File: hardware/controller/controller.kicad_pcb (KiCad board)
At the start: 4 copper layers, 57 x 47 mm, 46 parts, among them J1 Conn_01x02_Pin, J11 Barrel_Jack, J12 USB_C_Receptacle_USB2.0_14P, J2 Conn_01x02_Pin, J3 Conn_01x02_Pin, J5 Screw_Terminal_01x02, J6 Screw_Terminal_01x02, U1 ESP32-C3-MINI-1, U2 MAX31855KASA, U3 MAX31855KASA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

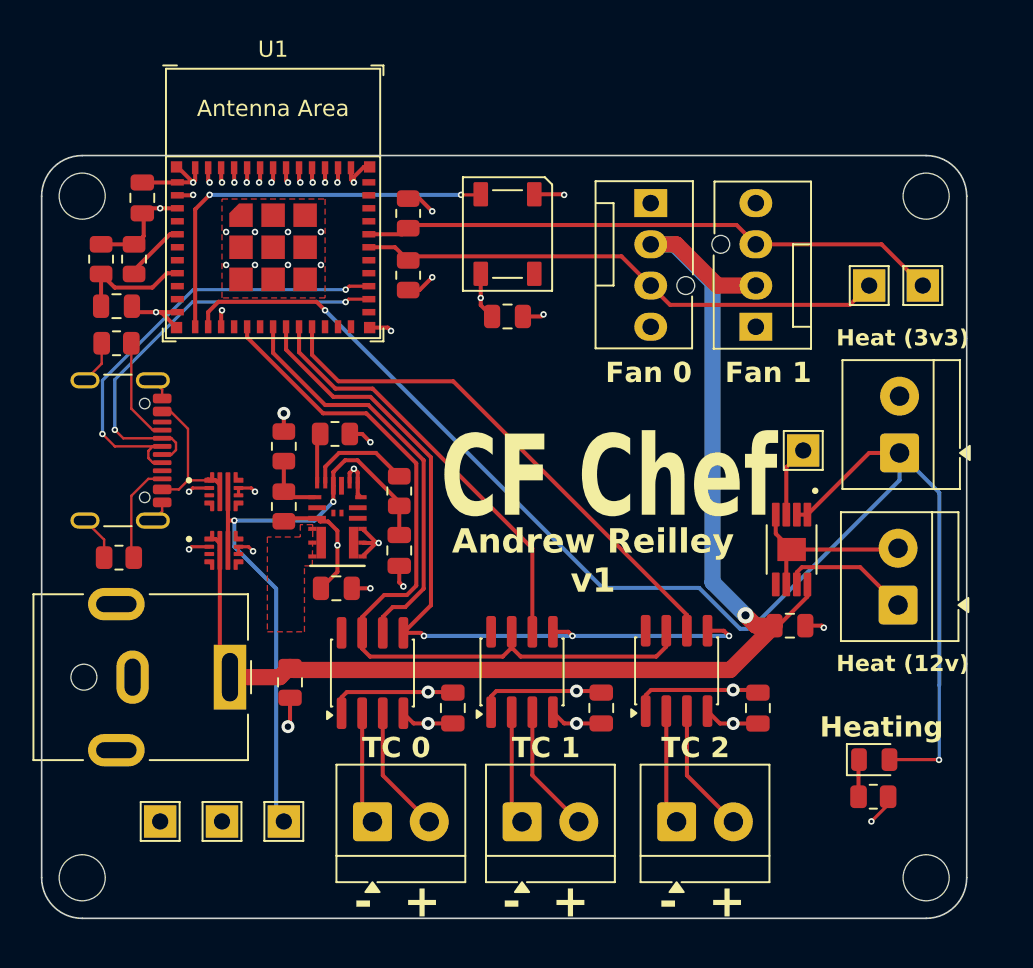
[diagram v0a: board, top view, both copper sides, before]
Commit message: Reroute USB connector
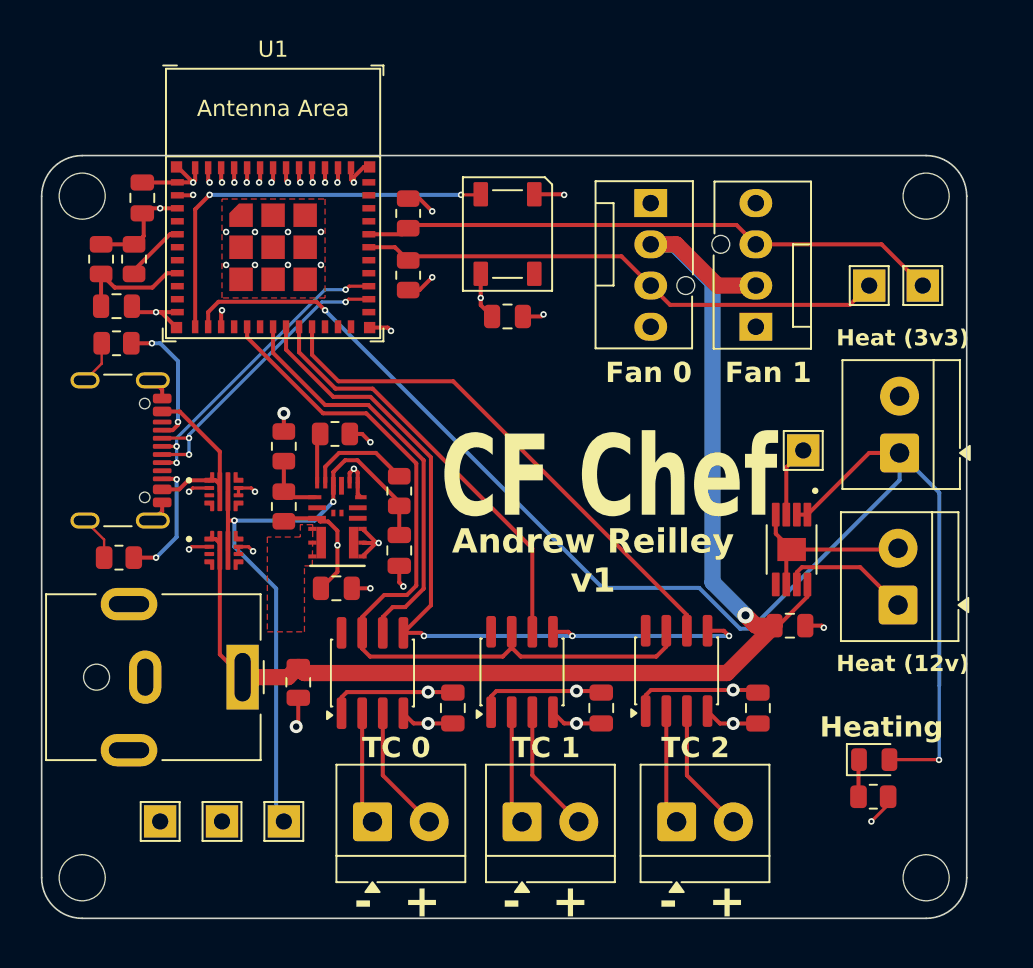
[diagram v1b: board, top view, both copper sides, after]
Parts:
- moved J11 0.78 mm to (119.6, 104.1)
- moved C2 0.51 mm to (123.1, 104.5)
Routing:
- net /Microcontroller/USB_D+: track 28.5 -> 19.0 mm, vias 2 -> 3
- net /Microcontroller/USB_D-: track 26.3 -> 19.1 mm, vias 2 -> 3
- net Net-(J12-CC1): track 6.48 -> 8.37 mm, vias 0 -> 2
- net +5V: track 9.65 -> 11.4 mm
- net Net-(J12-CC2): track 6.20 -> 7.84 mm, vias 0 -> 2

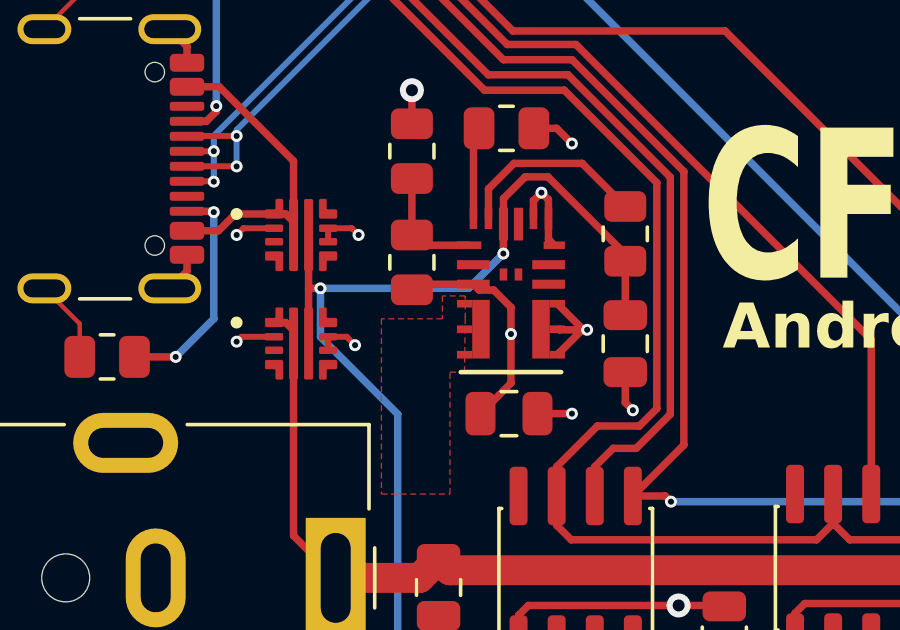
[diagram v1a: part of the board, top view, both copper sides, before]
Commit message: Fix some DRC errors
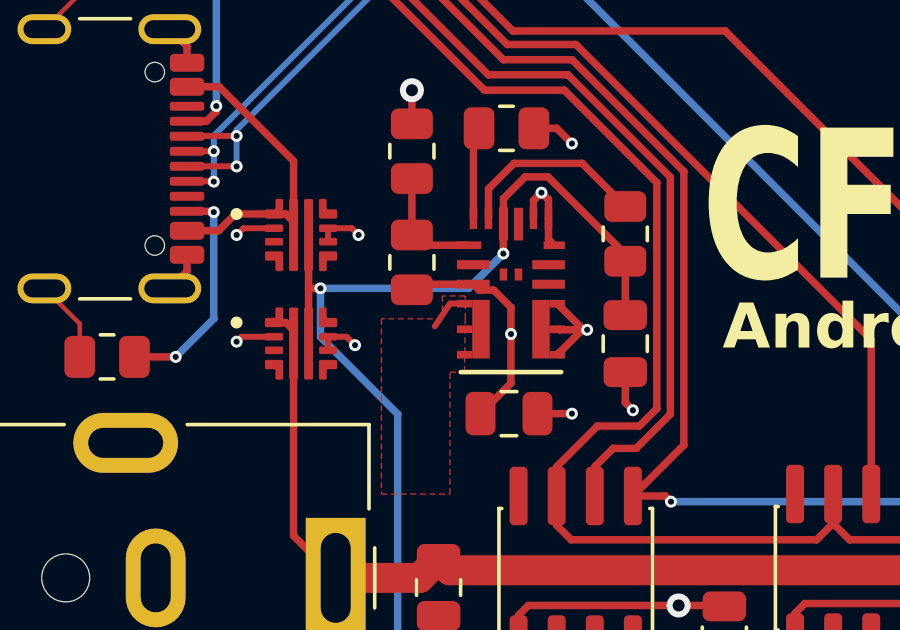
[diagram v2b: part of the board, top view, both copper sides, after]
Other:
- board text removed: "${REFERENCE}"
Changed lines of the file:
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@@
 		(sheetname "/Power/")
 		(sheetfile "power.kicad_sch")
+		(clearance 0.08)
 		(attr smd)
 		(fp_poly
@@
 		(sheetname "/Power/")
 		(sheetfile "power.kicad_sch")
+		(clearance 0.08)
 		(attr smd)
 		(fp_poly
@@
 		(sheetname "/Power/")
 		(sheetfile "power.kicad_sch")
+		(clearance 0.08)
 		(attr smd)
 		(fp_poly
@@
 			(layer "F.CrtYd")
 		)
-		(fp_text user "${REFERENCE}"
-			(at 0 -2 0)
-			(layer "F.Fab")
-			(effects
-				(font
-					(size 1 1)
-					(thickness 0.15)
-				)
-			)
-		)
 		(pad "1" thru_hole rect
 			(at 0 0)
@@
 		(sheetname "/Microcontroller/")
 		(sheetfile "mcu.kicad_sch")
+		(clearance 0.01)
 		(attr smd)
 		(fp_line
@@
 	)
 	(gr_line
+		(start 123.952 94.996)
+		(end 123.444 94.996)
+		(stroke
+			(width 0.2)
+			(type default)
+		)
+		(layer "F.Cu")
+		(net 66)
+	)
+	(gr_line
+		(start 123.444 94.996)
+		(end 122.936 95.758)
+		(stroke
+			(width 0.2)
+			(type default)
+		)
+		(layer "F.Cu")
+		(net 66)
+	)
+	(gr_line
 		(start 107.25 116.5)
 		(end 107.25 74.5)
@@
 		)
 	)
-	(gr_text "${REFERENCE}"
-		(at 117.475 111.03 0)
-		(layer "F.Fab")
-		(effects
-			(font
-				(size 1 1)
-				(thickness 0.15)
-			)
-		)
-	)
-	(gr_text "${REFERENCE}"
-		(at 113.665 111.03 0)
-		(layer "F.Fab")
-		(effects
-			(font
-				(size 1 1)
-				(thickness 0.15)
-			)
-		)
-	)
 	(segment
 		(start 153.46 96.275)
@@
 			)
 		)
-	)
-	(zone
-		(net 0)
-		(net_name "")
-		(layer "F.Cu")
-		(hatch edge 0.5)
-		(connect_pads
-			(clearance 0)
-		)
-		(min_thickness 0.25)
-		(filled_areas_thickness no)
-		(keepout
-			(tracks not_allowed)
-			(vias not_allowed)
-			(pads not_allowed)
-			(copperpour not_allowed)
-			(footprints allowed)
-		)
-		(placement
-			(enabled no)
-			(sheetname "/Microcontroller/")
-		)
-		(fill
-			(thermal_gap 0.5)
-			(thermal_bridge_width 0.5)
-		)
-		(polygon
-			(pts
-				(xy 107.442 86.36) (xy 114.046 86.36) (xy 114.046 93.98) (xy 107.442 93.98)
-			)
-		)

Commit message: Zain PCB review
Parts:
- added H1: MountingHole, MountingHole:MountingHole_2.2mm_M2_ISO14580_Pad, F.Cu at (161.8, 74.5)
- added H2: MountingHole, MountingHole:MountingHole_2.2mm_M2_ISO14580_Pad, F.Cu at (109.8, 74.5)
- added H3: MountingHole, MountingHole:MountingHole_2.2mm_M2_ISO14580_Pad, F.Cu at (109.8, 116.5)
- added H4: MountingHole, MountingHole:MountingHole_2.2mm_M2_ISO14580_Pad, F.Cu at (161.8, 116.5)
- J7: renamed from Fan 0
- J8: renamed from Fan 1
- moved R5 1.50 mm to (111.9, 79.5), turned to 180 degrees
- moved R6 1.38 mm to (111.9, 77.5), turned to 180 degrees
- moved C6 1.02 mm to (140.7, 106.1)
- moved C3 1.02 mm to (150.4, 106.0)
- moved C4 1.02 mm to (131.6, 106.0)
- moved C7 0.25 mm to (111.9, 81.5)
- renumbered Heating to D2
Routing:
- net GND: track 97.7 -> 77.7 mm, vias 41 -> 46
- net Net-(U1-EN/CHIP_PU): track 7.40 -> 5.72 mm
- net Net-(U1-GPIO2/ADC1_CH2): track 3.81 -> 3.05 mm
- net +3V3: vias 10 -> 11
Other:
- outline, holes or cut-outs redrawn

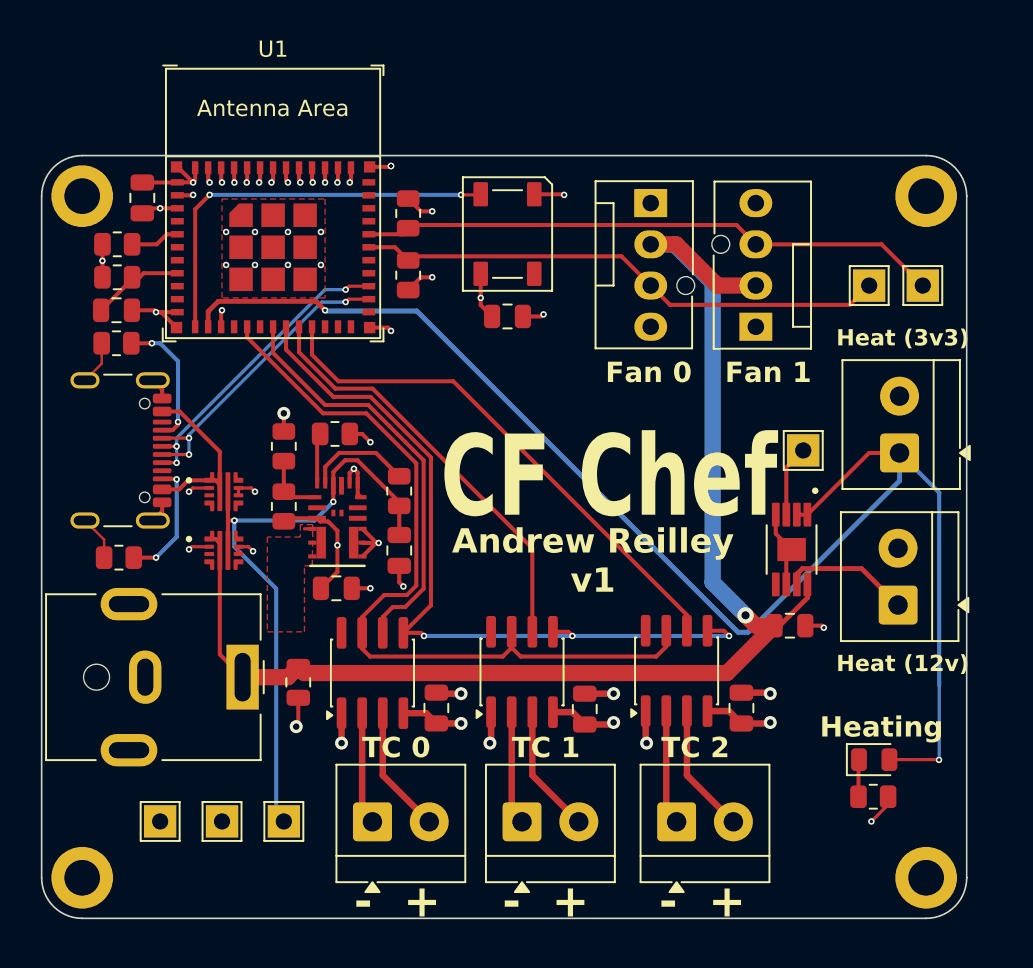
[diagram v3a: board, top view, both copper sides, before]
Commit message: Route missed trace, add some vias
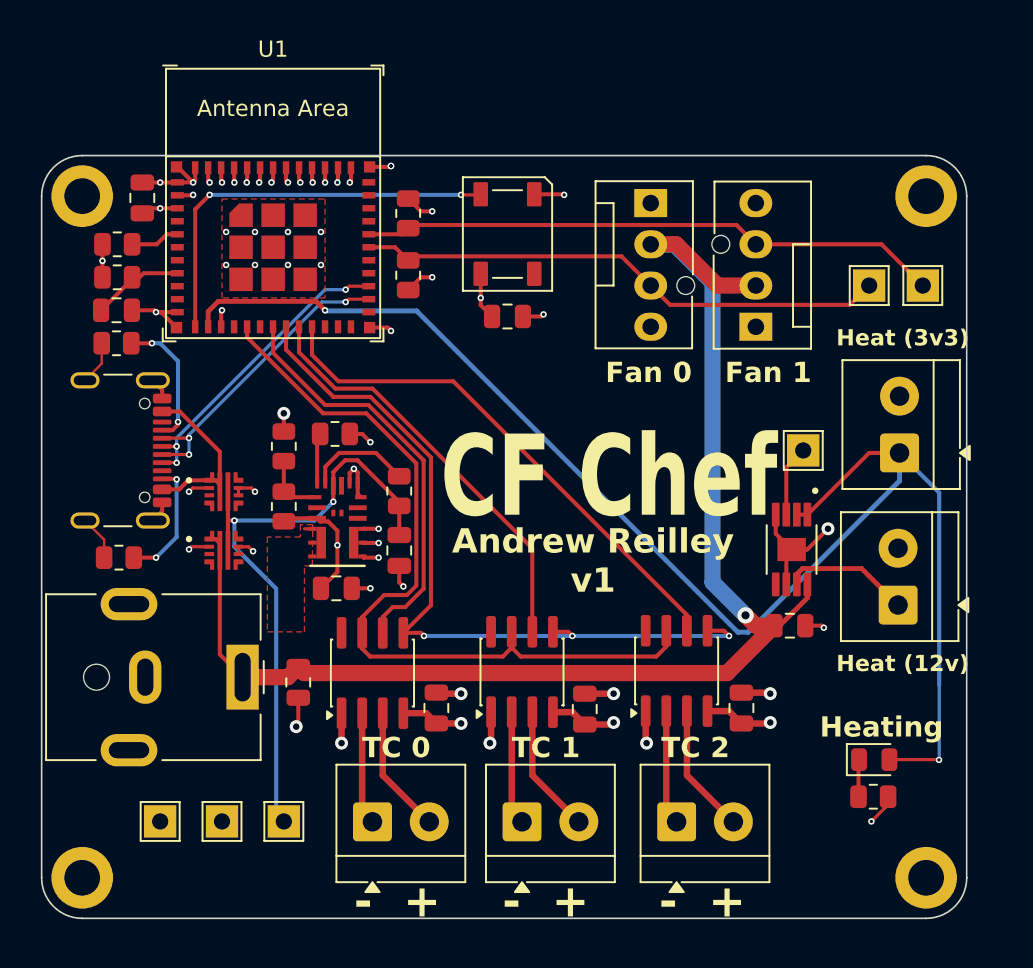
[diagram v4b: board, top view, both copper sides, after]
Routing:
- net GND: track 77.7 -> 80.5 mm, vias 46 -> 48
- net +3V3: track 28.8 -> 28.4 mm, vias 11 -> 13
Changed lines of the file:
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@@
+	)
+	(segment
+		(start 154.423 96.275)
+		(end 155.702 94.996)
+		(width 0.25)
+		(layer "F.Cu")
+		(net 18)
 	)
 	(segment
@@
 	)
 	(segment
+		(start 153.46 96.275)
+		(end 154.423 96.275)
+		(width 0.25)
+		(layer "F.Cu")
+		(net 18)
+	)
+	(segment
 		(start 150.368 105.095)
 		(end 152.085 105.095)
@@
 		(drill 0.2)
 		(layers "F.Cu" "B.Cu")
+		(net 18)
+	)
+	(via
+		(at 114.554 73.66)
+		(size 0.4)
+		(drill 0.2)
+		(layers "F.Cu" "B.Cu")
+		(free yes)
 		(net 18)
 	)
@@
 	)
 	(via
+		(at 155.702 94.996)
+		(size 0.8)
+		(drill 0.4)
+		(layers "F.Cu" "B.Cu")
+		(net 18)
+	)
+	(via
 		(at 120.396 78.74)
 		(size 0.4)
@@
 	)
 	(segment
+		(start 127.094 94.996)
+		(end 127.094 95.001)
+		(width 0.25)
+		(layer "F.Cu")
+		(net 21)
+	)
+	(segment
+		(start 127.095 96.774)
+		(end 127.094 96.773)
+		(width 0.25)
+		(layer "F.Cu")
+		(net 21)
+	)
+	(segment
 		(start 130.622 75.438)
 		(end 129.8365 74.6525)
@@
 	)
 	(segment
-		(start 127.094 96.629)
-		(end 127.094 96.701)
+		(start 128.016 94.996)
+		(end 127.094 94.996)
 		(width 0.25)
 		(layer "F.Cu")
@@
 	)
 	(segment
+		(start 127.094 96.773)
+		(end 127.094 96.701)
+		(width 0.25)
+		(layer "F.Cu")
+		(net 21)
+	)
+	(segment
 		(start 110.998 78.486)
 		(end 110.998 79.502)
@@
 	)
 	(segment
-		(start 127.852 95.871)
-		(end 127.094 96.629)
-		(width 0.25)
-		(layer "F.Cu")
-		(net 21)
-	)
-	(segment
-		(start 127.094 95.073)
-		(end 127.094 95.001)
+		(start 128.016 96.774)
+		(end 127.095 96.774)
 		(width 0.25)
 		(layer "F.Cu")
@@
 		(start 134.306 81.215)
 		(end 135.006 81.915)
-		(width 0.25)
-		(layer "F.Cu")
-		(net 21)
-	)
-	(segment
-		(start 127.892 95.871)
-		(end 127.094 95.073)
 		(width 0.25)
 		(layer "F.Cu")
@@
 	)
 	(via
+		(at 128.016 94.996)
+		(size 0.4)
+		(drill 0.2)
+		(layers "F.Cu" "B.Cu")
+		(free yes)
+		(net 21)
+	)
+	(via
 		(at 127.508 98.665)
 		(size 0.4)
@@
 		(net 21)
 	)
+	(via
+		(at 128.016 96.774)
+		(size 0.4)
+		(drill 0.2)
+		(layers "F.Cu" "B.Cu")
+		(free yes)
+		(net 21)
+	)

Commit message: Add serial number box
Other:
- board text added: "#"
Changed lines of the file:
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@@
 			)
 		)
+		(property "FT Rotation Offset" "-90"
+			(at 0 0 270)
+			(unlocked yes)
+			(layer "F.Fab")
+			(hide yes)
+			(effects
+				(font
+					(size 1 1)
+					(thickness 0.15)
+				)
+			)
+		)
 		(sheetname "/Microcontroller/")
 		(sheetfile "mcu.kicad_sch")
@@
 		)
 	)
+	(gr_text "#"
+		(at 147.828 97.028 0)
+		(layer "B.SilkS")
+		(effects
+			(font
+				(size 5 5)
+				(thickness 0.8)
+				(bold yes)
+			)
+			(justify left bottom mirror)
+		)
+	)
 	(segment
 		(start 126.726 92.157)
@@
 			)
 		)
+	)
+	(zone
+		(net 0)
+		(net_name "")
+		(layer "B.SilkS")
+		(hatch edge 0.5)
+		(connect_pads
+			(clearance 0.5)
+		)
+		(min_thickness 0.25)
+		(filled_areas_thickness no)
+		(fill yes
+			(thermal_gap 0.5)
+			(thermal_bridge_width 0.5)
+		)
+		(polygon
+			(pts
+				(xy 117.348 90.17) (xy 141.732 90.17) (xy 141.732 97.79) (xy 117.348 97.79)
+			)
+		)
